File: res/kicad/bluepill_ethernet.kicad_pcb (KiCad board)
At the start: 2 copper layers, 12 parts, among them J2 Conn_01x03, U1 BluePill_STM32F103C, U2 93C46, U3 WIZ850io

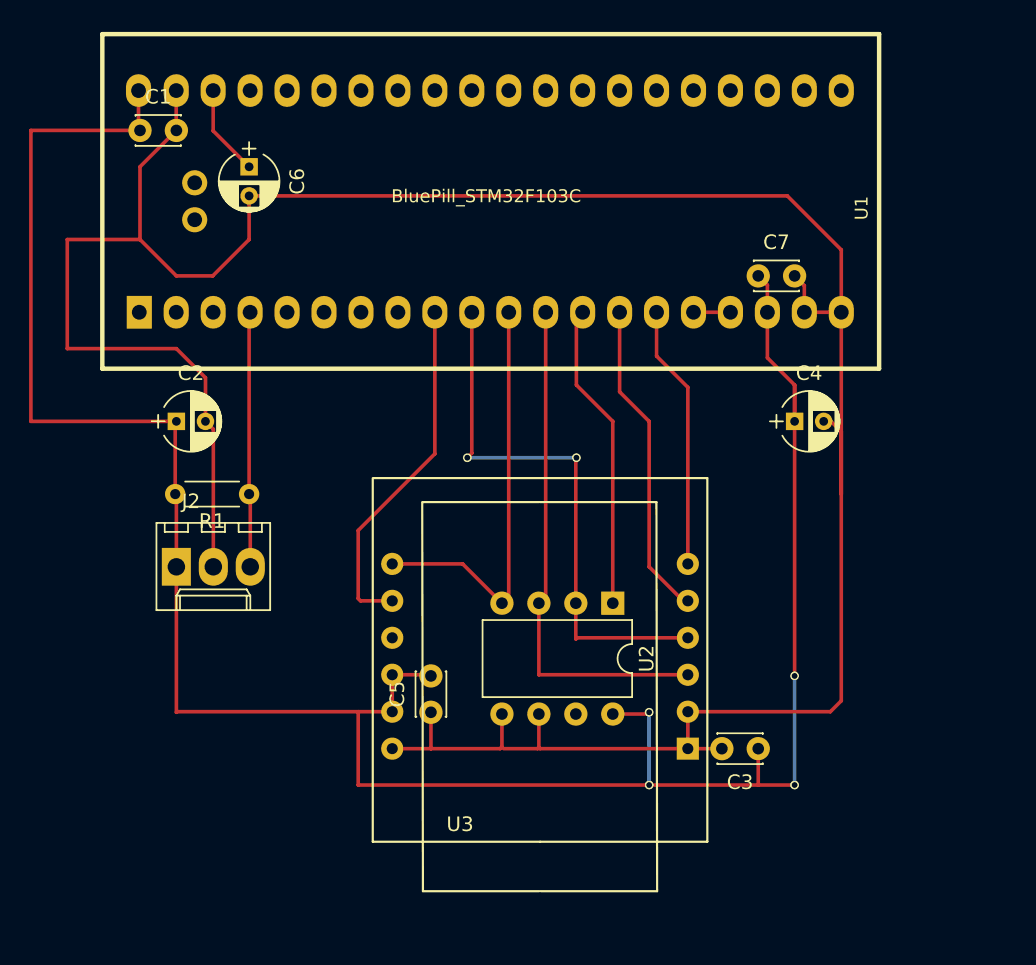
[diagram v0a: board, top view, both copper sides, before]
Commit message: Add revision information for kicad circuit (rev1)
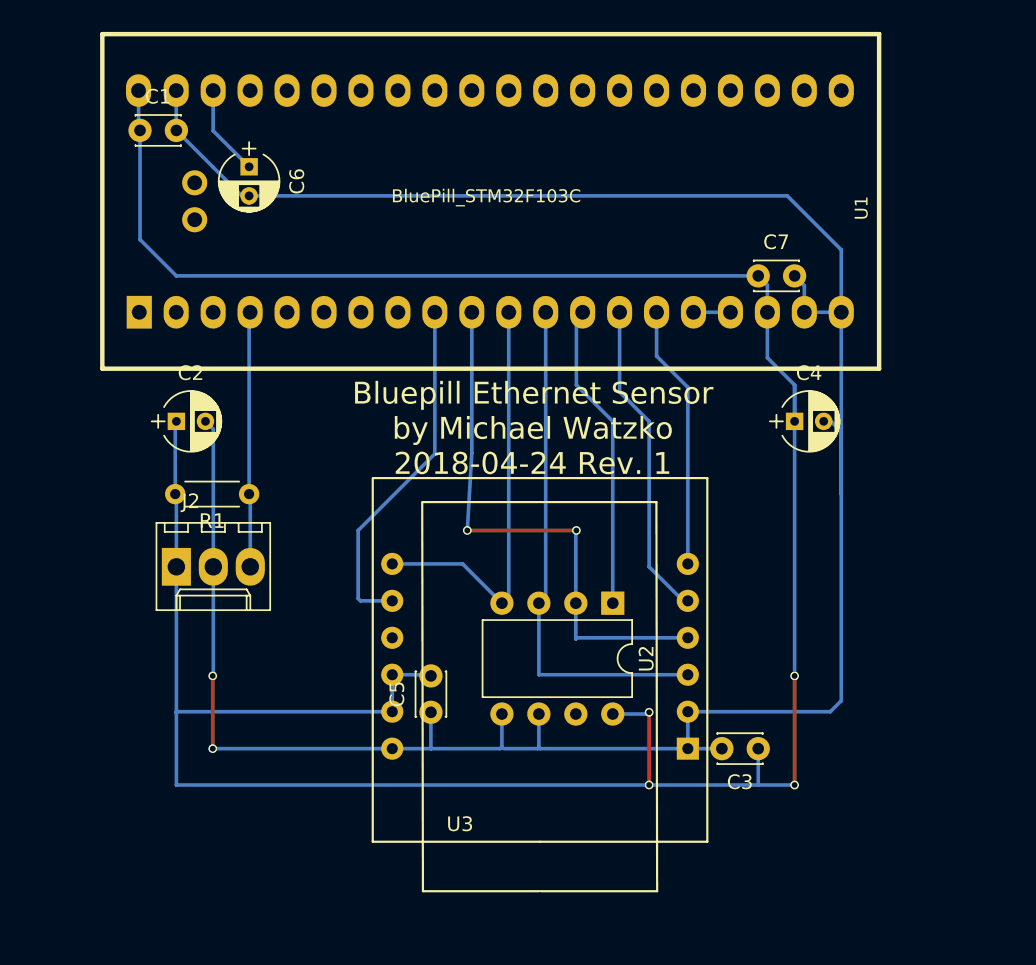
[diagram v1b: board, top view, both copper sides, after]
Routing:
- net VCC: track 164.3 -> 190.3 mm
- net GND: track 187.9 -> 173.4 mm, vias 0 -> 2
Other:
- board text added: "Bluepill Ethernet Sensor by Michael Watzko 2018-04-24 Rev. 1"

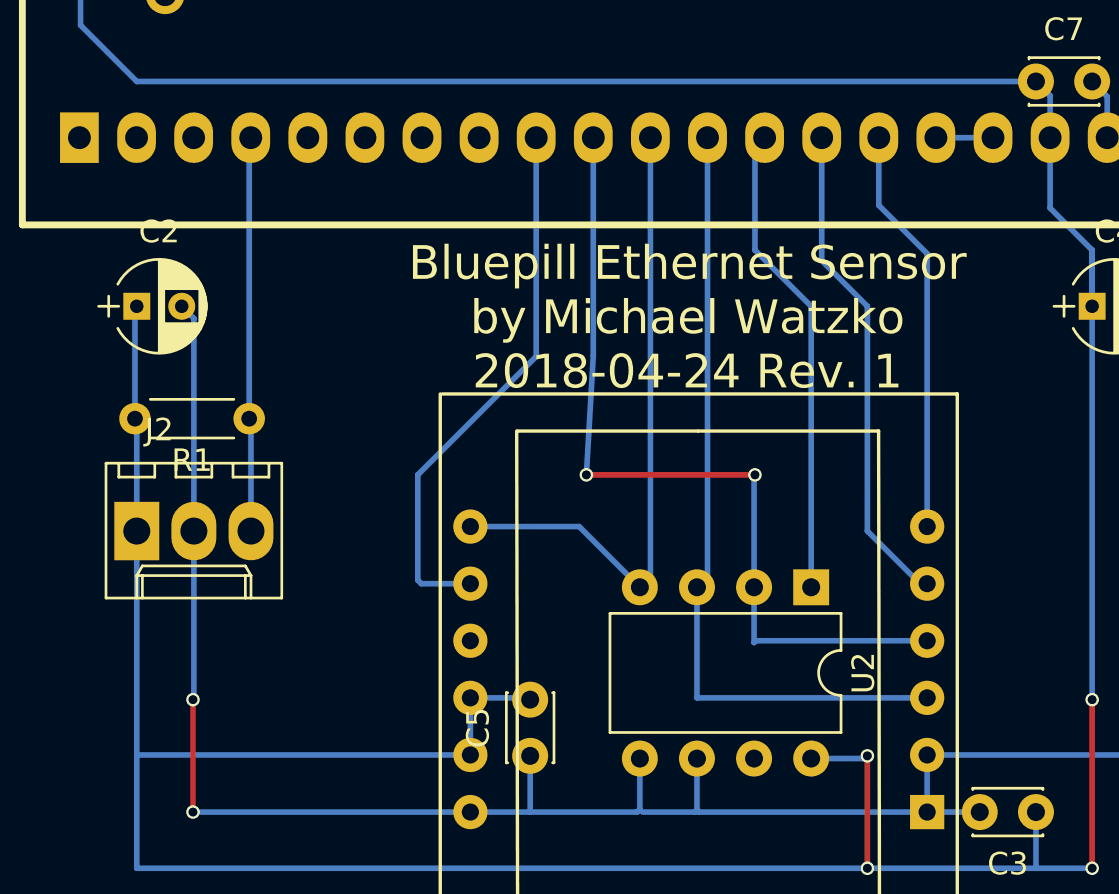
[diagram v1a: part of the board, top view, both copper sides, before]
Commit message: Add button to kicad circuit for 'factory reset' the configuration (delete eeprom)
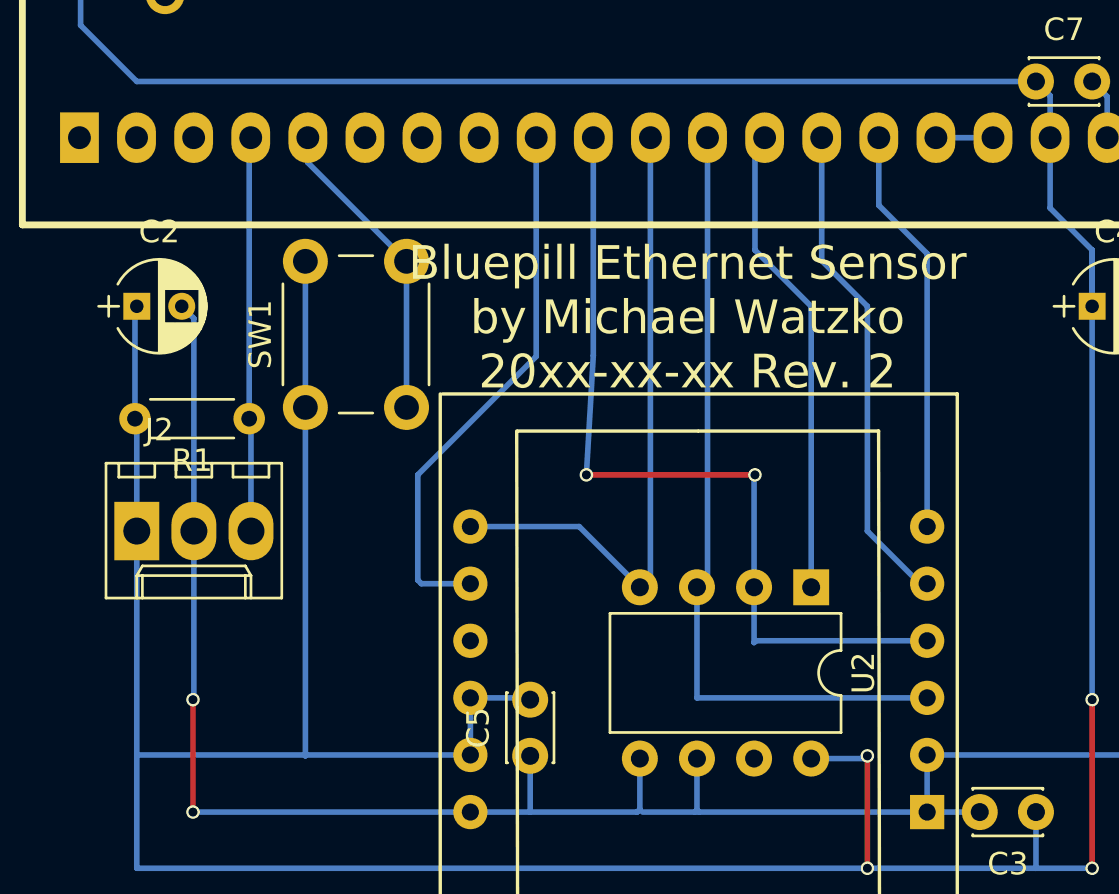
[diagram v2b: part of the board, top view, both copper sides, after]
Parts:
- added SW1: SW_Push, Buttons_Switches_THT:SW_PUSH_6mm, F.Cu at (50.0, 57.0)
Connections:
- U1 pad 5: (no net) -> Net-(SW1-Pad2)
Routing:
- net VCC: track 190.3 -> 212.4 mm
- net Net-(SW1-Pad2): track 0.00 -> 13.8 mm
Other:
- board text added: "Bluepill Ethernet Sensor by Michael Watzko 20xx-xx-xx Rev. 2"
- board text removed: "Bluepill Ethernet Sensor by Michael Watzko 2018-04-24 Rev. 1"
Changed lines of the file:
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@@
     (thickness 1.6)
     (drawings 1)
-    (tracks 119)
+    (tracks 127)
     (zones 0)
-    (modules 12)
-    (nets 13)
+    (modules 13)
+    (nets 14)
   )
   (page A4)
@@
   (net 11 "Net-(U1-Pad16)")
   (net 12 "Net-(C6-Pad1)")
+  (net 13 "Net-(SW1-Pad2)")
   (net_class Default "Dies ist die voreingestellte Netzklasse."
     (clearance 0.2)
@@
     (add_net "Net-(C6-Pad1)")
     (add_net "Net-(J2-Pad3)")
+    (add_net "Net-(SW1-Pad2)")
     (add_net "Net-(U1-Pad10)")
     (add_net "Net-(U1-Pad11)")
@@
     (pad 4 thru_hole oval (at 0 7.5692) (size 1.7272 2.25) (drill 1.016) (layers *.Cu *.Mask F.SilkS)
       (net 3 "Net-(J2-Pad3)"))
-    (pad 5 thru_hole oval (at 0 10.1092) (size 1.7272 2.25) (drill 1.016) (layers *.Cu *.Mask F.SilkS))
+    (pad 5 thru_hole oval (at 0 10.1092) (size 1.7272 2.25) (drill 1.016) (layers *.Cu *.Mask F.SilkS)
+      (net 13 "Net-(SW1-Pad2)"))
     (pad 6 thru_hole oval (at 0 12.6492) (size 1.7272 2.25) (drill 1.016) (layers *.Cu *.Mask F.SilkS))
     (pad 7 thru_hole oval (at 0 15.1892) (size 1.7272 2.25) (drill 1.016) (layers *.Cu *.Mask F.SilkS))
@@
     )
   )
-  (gr_text "Bluepill Ethernet Sensor\nby Michael Watzko\n2018-04-24 Rev. 1" (at 67 53) (layer F.SilkS)
+  (module Buttons_Switches_THT:SW_PUSH_6mm (layer F.Cu)
+    (at 50 57 90)
+    (descr https://www.omron.com/ecb/products/pdf/en-b3f.pdf)
+    (tags "tact sw push 6mm")
+    (fp_text reference SW1 (at 3.25 -2 90) (layer F.SilkS)
+      (effects (font (size 1 1) (thickness 0.15)))
+    )
+    (fp_text value SW_Push (at 3.75 6.7 90) (layer F.Fab)
+      (effects (font (size 1 1) (thickness 0.15)))
+    )
+    (fp_circle (center 3.25 2.25) (end 1.25 2.5) (layer F.Fab) (width 0.1))
+    (fp_line (start 6.75 3) (end 6.75 1.5) (layer F.SilkS) (width 0.12))
+    (fp_line (start 5.5 -1) (end 1 -1) (layer F.SilkS) (width 0.12))
+    (fp_line (start -0.25 1.5) (end -0.25 3) (layer F.SilkS) (width 0.12))
+    (fp_line (start 1 5.5) (end 5.5 5.5) (layer F.SilkS) (width 0.12))
+    (fp_line (start 8 -1.25) (end 8 5.75) (layer F.CrtYd) (width 0.05))
+    (fp_line (start 7.75 6) (end -1.25 6) (layer F.CrtYd) (width 0.05))
+    (fp_line (start -1.5 5.75) (end -1.5 -1.25) (layer F.CrtYd) (width 0.05))
+    (fp_line (start -1.25 -1.5) (end 7.75 -1.5) (layer F.CrtYd) (width 0.05))
+    (fp_line (start -1.5 6) (end -1.25 6) (layer F.CrtYd) (width 0.05))
+    (fp_line (start -1.5 5.75) (end -1.5 6) (layer F.CrtYd) (width 0.05))
+    (fp_line (start -1.5 -1.5) (end -1.25 -1.5) (layer F.CrtYd) (width 0.05))
+    (fp_line (start -1.5 -1.25) (end -1.5 -1.5) (layer F.CrtYd) (width 0.05))
+    (fp_line (start 8 -1.5) (end 8 -1.25) (layer F.CrtYd) (width 0.05))
+    (fp_line (start 7.75 -1.5) (end 8 -1.5) (layer F.CrtYd) (width 0.05))
+    (fp_line (start 8 6) (end 8 5.75) (layer F.CrtYd) (width 0.05))
+    (fp_line (start 7.75 6) (end 8 6) (layer F.CrtYd) (width 0.05))
+    (fp_line (start 0.25 -0.75) (end 3.25 -0.75) (layer F.Fab) (width 0.1))
+    (fp_line (start 0.25 5.25) (end 0.25 -0.75) (layer F.Fab) (width 0.1))
+    (fp_line (start 6.25 5.25) (end 0.25 5.25) (layer F.Fab) (width 0.1))
+    (fp_line (start 6.25 -0.75) (end 6.25 5.25) (layer F.Fab) (width 0.1))
+    (fp_line (start 3.25 -0.75) (end 6.25 -0.75) (layer F.Fab) (width 0.1))
+    (fp_text user %R (at 3.25 2.25 90) (layer F.Fab)
+      (effects (font (size 1 1) (thickness 0.15)))
+    )
+    (pad 1 thru_hole circle (at 6.5 0 180) (size 2 2) (drill 1.1) (layers *.Cu *.Mask)
+      (net 1 VCC))
+    (pad 2 thru_hole circle (at 6.5 4.5 180) (size 2 2) (drill 1.1) (layers *.Cu *.Mask)
+      (net 13 "Net-(SW1-Pad2)"))
+    (pad 1 thru_hole circle (at 0 0 180) (size 2 2) (drill 1.1) (layers *.Cu *.Mask)
+      (net 1 VCC))
+    (pad 2 thru_hole circle (at 0 4.5 180) (size 2 2) (drill 1.1) (layers *.Cu *.Mask)
+      (net 13 "Net-(SW1-Pad2)"))
+    (model ${KISYS3DMOD}/Buttons_Switches_THT.3dshapes/SW_PUSH_6mm.wrl
+      (offset (xyz 0.1269999980926514 0 0))
+      (scale (xyz 0.3937 0.3937 0.3937))
+      (rotate (xyz 0 0 0))
+    )
+  )
+  (gr_text "Bluepill Ethernet Sensor\nby Michael Watzko\n20xx-xx-xx Rev. 2" (at 67 53) (layer F.SilkS)
     (effects (font (size 1.5 1.5) (thickness 0.3)))
   )
+  (segment (start 50 57) (end 50 72.46) (width 0.25) (layer B.Cu) (net 1) (status 400000))
+  (segment (start 50 72.46) (end 50 72.5) (width 0.25) (layer B.Cu) (net 1))
+  (segment (start 50 72.5) (end 50 72.46) (width 0.25) (layer B.Cu) (net 1))
+  (segment (start 50 50.5) (end 50 57) (width 0.25) (layer B.Cu) (net 1) (status C00000))
   (segment (start 40 32.5) (end 40 40) (width 0.25) (layer B.Cu) (net 1) (status 400000))
   (segment (start 42.5 42.5) (end 82.5 42.5) (width 0.25) (layer B.Cu) (net 1) (status 800000))
@@
   (segment (start 85 77.5) (end 85 70) (width 0.25) (layer F.Cu) (net 1))
   (via (at 85 77.5) (size 0.6) (drill 0.4) (layers F.Cu B.Cu) (net 1))
-  (segment (start 57.34 72.46) (end 42.54 72.46) (width 0.25) (layer B.Cu) (net 1) (status 400000))
+  (segment (start 57.34 72.46) (end 50 72.46) (width 0.25) (layer B.Cu) (net 1) (status 400000))
+  (segment (start 50 72.46) (end 42.54 72.46) (width 0.25) (layer B.Cu) (net 1))
   (segment (start 74.88 72.62) (end 72.5 72.62) (width 0.25) (layer B.Cu) (net 1))
   (segment (start 75 72.5) (end 74.88 72.62) (width 0.25) (layer B.Cu) (net 1))
@@
   (segment (start 45.0292 32.5292) (end 45.0292 29.76) (width 0.25) (layer B.Cu) (net 12) (status 800020))
   (segment (start 47.5 35) (end 45.0292 32.5292) (width 0.25) (layer B.Cu) (net 12))
+  (segment (start 50.1092 45) (end 50.1092 46.1092) (width 0.25) (layer B.Cu) (net 13) (status C00000))
+  (segment (start 50.1092 46.1092) (end 54.5 50.5) (width 0.25) (layer B.Cu) (net 13) (status C00000))
+  (segment (start 54.5 50.5) (end 54.5 57) (width 0.25) (layer B.Cu) (net 13) (status C00000))
 )

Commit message: Revision 2.0
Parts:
- added D1: LED, LEDs:LED_D3.0mm, F.Cu at (48.5, 53.3)
- added D2: LED, LEDs:LED_D3.0mm, F.Cu at (53.3, 53.3)
- added D3: LED, LEDs:LED_D3.0mm, F.Cu at (58.2, 53.3)
- added J1: HEADER-1x20, Pin_Headers:Pin_Header_Straight_1x20_Pitch2.54mm, F.Cu at (39.9, 26.9)
- added R2: R, Resistors_THT:R_Axial_DIN0204_L3.6mm_D1.6mm_P5.08mm_Horizontal, F.Cu at (56.0, 39.0)
- added R3: R, Resistors_THT:R_Axial_DIN0204_L3.6mm_D1.6mm_P5.08mm_Horizontal, F.Cu at (53.0, 39.0)
- added R4: R, Resistors_THT:R_Axial_DIN0204_L3.6mm_D1.6mm_P5.08mm_Horizontal, F.Cu at (48.5, 56.1)
- added R5: R, Resistors_THT:R_Axial_DIN0204_L3.6mm_D1.6mm_P5.08mm_Horizontal, F.Cu at (51.1, 56.1)
- added R6: R, Resistors_THT:R_Axial_DIN0204_L3.6mm_D1.6mm_P5.08mm_Horizontal, F.Cu at (53.6, 56.1)
- moved SW1 13.5 mm to (49.5, 70.5)
- moved C3 7.32 mm to (75.2, 74.9), turned to 90 degrees
- moved C2 2.50 mm to (40.0, 52.5)
- moved J2 2.50 mm to (40.0, 62.5)
- moved R1 2.50 mm to (45.0, 57.5)
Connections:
- U1 pad 21: (no net) -> Net-(J1-Pad20)
- U1 pad 22: (no net) -> Net-(J1-Pad19)
- U1 pad 23: (no net) -> Net-(J1-Pad18)
- U1 pad 24: (no net) -> Net-(J1-Pad17)
- U1 pad 25: (no net) -> Net-(J1-Pad16)
- U1 pad 26: (no net) -> Net-(J1-Pad15)
- U1 pad 27: (no net) -> Net-(J1-Pad14)
- U1 pad 28: (no net) -> Net-(J1-Pad13)
- U1 pad 29: (no net) -> Net-(J1-Pad12)
- U1 pad 30: (no net) -> Net-(J1-Pad11)
- U1 pad 31: (no net) -> Net-(J1-Pad10)
- U1 pad 32: (no net) -> Net-(J1-Pad9)
- U1 pad 33: (no net) -> Net-(J1-Pad8)
- U1 pad 34: (no net) -> Net-(J1-Pad7)
- U1 pad 35: (no net) -> Net-(J1-Pad6)
- U1 pad 36: (no net) -> Net-(J1-Pad5)
- U1 pad 37: (no net) -> Net-(J1-Pad4)
- U1 pad 6: (no net) -> Net-(D1-Pad2)
- U1 pad 7: (no net) -> Net-(D2-Pad2)
- U1 pad 8: (no net) -> Net-(D3-Pad2)
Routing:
- net Net-(SW1-Pad2): track 13.8 -> 38.0 mm
- net VCC: track 212.4 -> 230.4 mm, vias 4 -> 2
- net GND: track 173.4 -> 183.1 mm
- net Net-(D1-Pad2): track 0.00 -> 7.51 mm
- net Net-(J1-Pad7): track 0.00 -> 7.36 mm
- net Net-(J1-Pad6): track 0.00 -> 7.17 mm
- net Net-(D2-Pad2): track 0.00 -> 6.57 mm
- net Net-(D3-Pad2): track 0.00 -> 5.98 mm
- net Net-(D3-Pad1): track 0.00 -> 5.73 mm
- net Net-(D2-Pad1): track 0.00 -> 3.74 mm
- net Net-(J2-Pad3): track 17.7 -> 20.8 mm
- net Net-(J1-Pad5): track 0.00 -> 2.87 mm
- net Net-(J1-Pad4): track 0.00 -> 2.87 mm
- net Net-(J1-Pad19): track 0.00 -> 2.87 mm
- net Net-(J1-Pad17): track 0.00 -> 2.87 mm
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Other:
- board text added: "Bluepill Ethernet Sensor by Michael Watzko 2018-05-31 Rev. 2"
- board text removed: "Bluepill Ethernet Sensor by Michael Watzko 20xx-xx-xx Rev. 2"
